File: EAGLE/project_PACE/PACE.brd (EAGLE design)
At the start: 114.5 x 63 mm, 34 parts, among them J3 PTH, U2 MPM3630GQV-P

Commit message: Replace micro usb with usb c
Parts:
- CAM1, CAM2, CAM3, CAM4: value 10118194-0001LF -> USB-C; device USB_Micro_B_v2:AMPHENOL_10118194-0001LF -> USB-C:USB-C
- moved CAM1 77.1 mm to (10.7, 46.0), turned to 270 degrees
- moved CAM2 74.2 mm to (10.7, 32.0), turned to 270 degrees
- moved CAM4 70.9 mm to (77.0, 7.11), turned to 0 degrees
- moved CAM3 70.1 mm to (76.7, 64.8), turned to 180 degrees
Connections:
- net 5VO: now also CAM1.A4, CAM1.A9, CAM2.A4, CAM2.A9, CAM3.A4, CAM3.A9, CAM4.A4, CAM4.A9; no longer CAM1.1, CAM2.1, CAM3.1, CAM4.1
- net GND: now also CAM1.B1, CAM1.B12, CAM2.B1, CAM2.B12, CAM3.B1, CAM3.B12, CAM4.B1, CAM4.B12; no longer CAM1.5, CAM2.5, CAM3.5, CAM4.5
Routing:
- net 5VO: track 234.1 -> 221.7 mm, vias 15 -> 11
- net GND: track 5.51 -> 0.00 mm, vias 17 -> 13

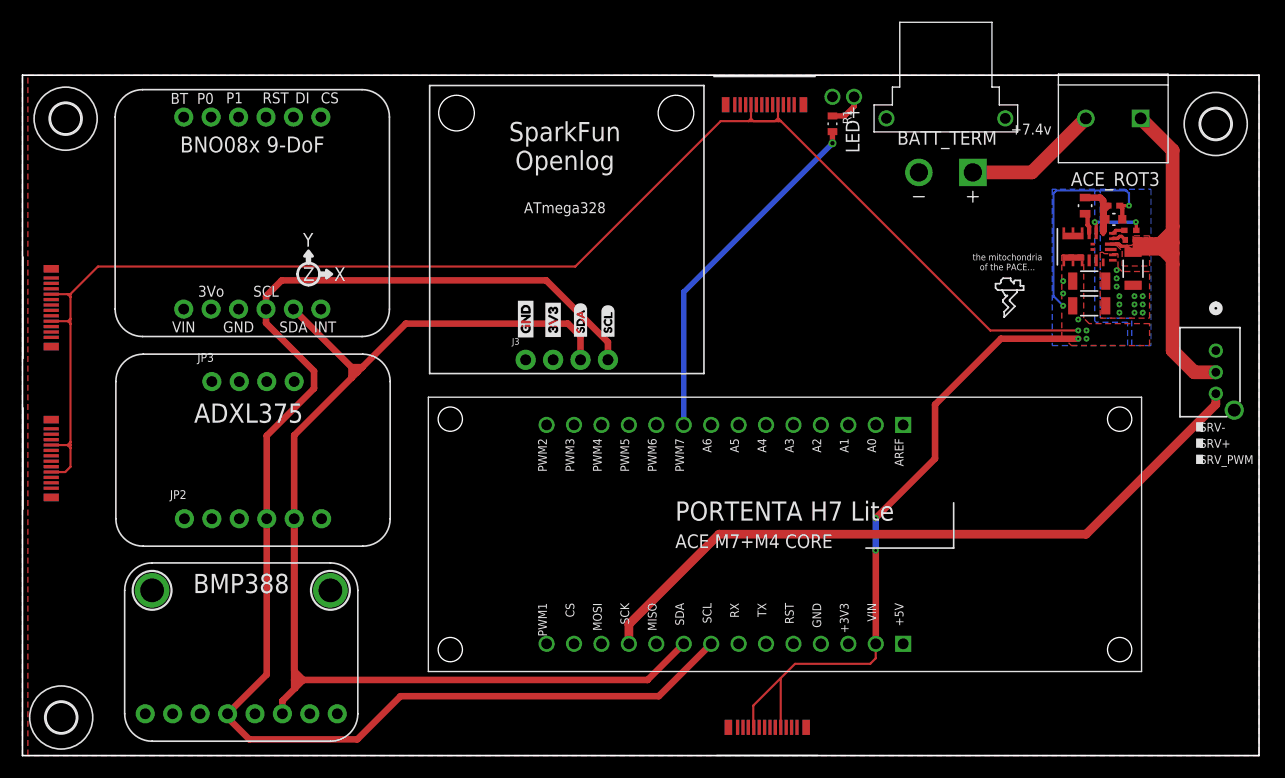
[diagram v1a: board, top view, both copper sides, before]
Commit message: Fix dimensions
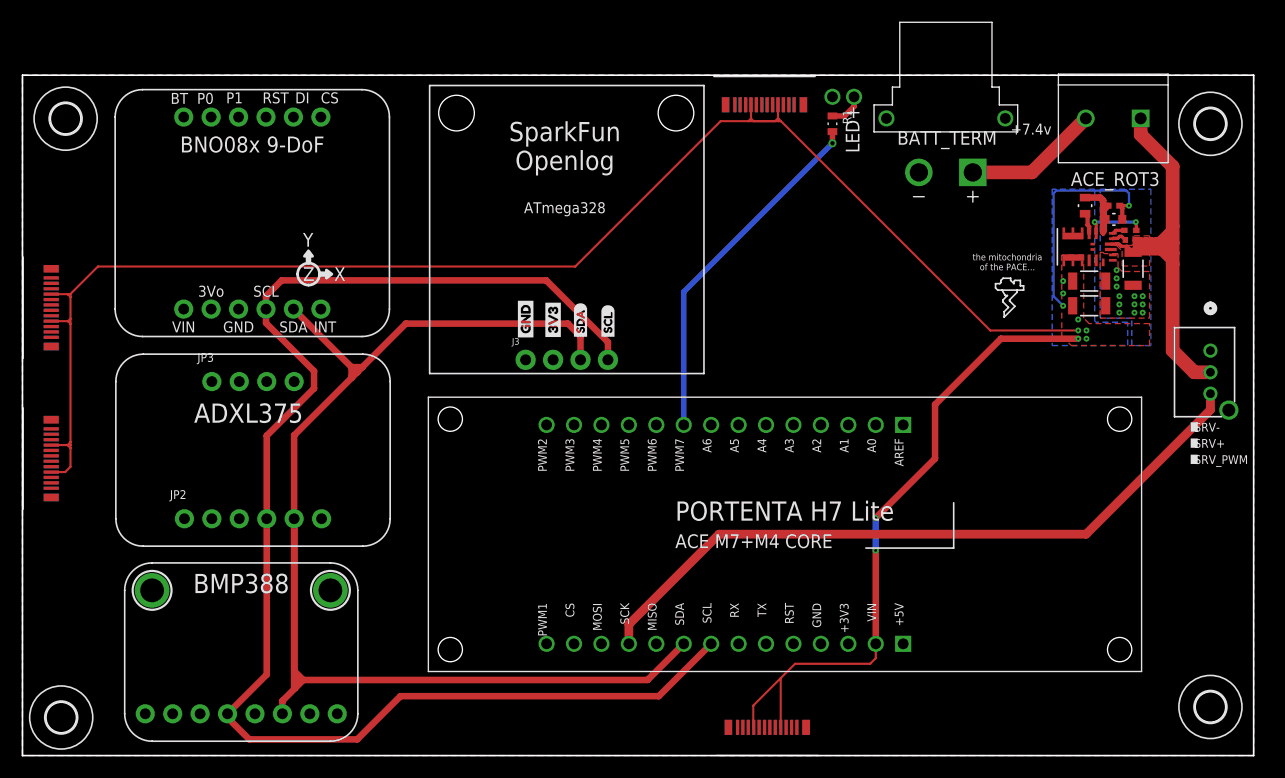
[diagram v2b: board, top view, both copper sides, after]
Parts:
- added U$29: (no value), holes:2,8
- moved SERVOCON 0.50 mm to (118.0, 42.0)
- moved U$14 0.49 mm to (118.0, 63.0)
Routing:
- net 7.4VCC: track 51.7 -> 51.2 mm
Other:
- board size 114.5 x 63 mm -> 114 x 63 mm
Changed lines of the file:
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@@
 <setting verticaltext="up"/>
 </settings>
-<grid distance="10" unitdist="mil" unit="mil" style="lines" multiple="1" display="yes" altdistance="5" altunitdist="mil" altunit="mil"/>
+<grid distance="0.5" unitdist="mm" unit="mm" style="lines" multiple="1" display="yes" altdistance="5" altunitdist="mil" altunit="mil"/>
 <layers>
 <layer number="1" name="Top" color="4" fill="1" visible="yes" active="yes"/>
@@
 <text x="23.885" y="35.321" size="1.778" layer="21">ADXL375</text>
 <dimension x1="22.5" y1="67.5" x2="22.5" y2="4.5" x3="-9" y3="36" textsize="1.778" layer="20"/>
-<wire x1="8" y1="67.5" x2="122.5" y2="67.5" width="0.15" layer="20"/>
-<wire x1="122.5" y1="67.5" x2="122.5" y2="4.5" width="0.15" layer="20"/>
-<wire x1="122.5" y1="4.5" x2="8" y2="4.5" width="0.15" layer="20"/>
+<wire x1="8" y1="67.5" x2="122" y2="67.5" width="0.15" layer="20"/>
+<wire x1="122" y1="67.5" x2="122" y2="4.5" width="0.15" layer="20"/>
+<wire x1="122" y1="4.5" x2="8" y2="4.5" width="0.15" layer="20"/>
 <wire x1="8" y1="4.5" x2="8" y2="67.5" width="0.15" layer="20"/>
 <text x="102.936" y="27.033" size="5.08" layer="22" font="vector" ratio="22" rot="MR45" align="center">P A C E</text>
@@
 ELEMENT</text>
 <text x="99.991" y="7.293" size="1.27" layer="22" font="vector" rot="MR45">v1.0 (now with more ports!)</text>
-<dimension x1="8" y1="67.5" x2="122.5" y2="67.5" x3="65.25" y3="74" textsize="1.778" layer="20"/>
 <text x="99.5" y="62" size="1.016" layer="21" font="vector">+7.4v</text>
-<text x="117" y="31.5" size="0.8128" layer="21" font="vector">SRV_PWM</text>
-<text x="117" y="33" size="0.8128" layer="21" font="vector">SRV+</text>
-<text x="117" y="34.5" size="0.8128" layer="21" font="vector">SRV-</text>
-<text x="116" y="34.5" size="5.08" layer="21" font="vector">.</text>
-<text x="116" y="33" size="5.08" layer="21" font="vector">.</text>
-<text x="116" y="31.5" size="5.08" layer="21" font="vector">.</text>
+<text x="116.5" y="31.5" size="0.8128" layer="21" font="vector">SRV_PWM</text>
+<text x="116.5" y="33" size="0.8128" layer="21" font="vector">SRV+</text>
+<text x="116.5" y="34.5" size="0.8128" layer="21" font="vector">SRV-</text>
+<text x="115.5" y="34.5" size="5.08" layer="21" font="vector">.</text>
+<text x="115.5" y="33" size="5.08" layer="21" font="vector">.</text>
+<text x="115.5" y="31.5" size="5.08" layer="21" font="vector">.</text>
 <text x="85.5" y="60.3" size="1.27" layer="21" font="vector" rot="R90">LED+</text>
 <text x="99.2" y="50.2" size="0.6096" layer="21" font="vector" align="center">the mitochondria
@@
 <wire x1="99.2" y1="47.1" x2="99" y2="47.1" width="0.1524" layer="21"/>
 <wire x1="99" y1="47.1" x2="98.7" y2="47.6" width="0.1524" layer="21"/>
+<dimension x1="8" y1="67.5" x2="122" y2="67.5" x3="65" y3="75.5" textsize="1.778" layer="20"/>
 </plain>
 <attributes>
@@
 <element name="U$10" library="ABX00042" package="MODULE_ABX00042_HEADERS" value="ABX00042_HEADERS_IO" x="78.603" y="24.984" smashed="yes" rot="R270"/>
 <element name="U$13" library="holes" library_urn="urn:adsk.eagle:library:237" package="2,8" package3d_urn="urn:adsk.eagle:package:14271/1" value="" x="11.996" y="63.476" smashed="yes"/>
-<element name="U$14" library="holes" library_urn="urn:adsk.eagle:library:237" package="2,8" package3d_urn="urn:adsk.eagle:package:14271/1" value="" x="118.489" y="62.984" smashed="yes"/>
+<element name="U$14" library="holes" library_urn="urn:adsk.eagle:library:237" package="2,8" package3d_urn="urn:adsk.eagle:package:14271/1" value="" x="118" y="63" smashed="yes"/>
 <element name="U$15" library="holes" library_urn="urn:adsk.eagle:library:237" package="2,8" package3d_urn="urn:adsk.eagle:package:14271/1" value="" x="11.586" y="8.026" smashed="yes"/>
 <element name="U$1" library="microbuilder" package="MOUNTINGHOLE_2.0_PLATED" value="MOUNTINGHOLE2.0" x="20.003" y="19.8" smashed="yes">
@@
 <element name="JP4" library="SparkFun" package="STAND-OFF" value="STAND-OFF" x="48.19" y="63.992" smashed="yes"/>
 <element name="JP5" library="SparkFun" package="STAND-OFF" value="STAND-OFF" x="68.51" y="63.992" smashed="yes"/>
-<element name="SERVOCON" library="3_Pin_JST_XA_Surface_Connector" package="CONN_B03B-PASK-1_(LF)_(SN)_JST" value="B03B-PASK-1_(LF)_(SN)" x="118.5" y="42" smashed="yes" rot="R270">
-<attribute name="COPYRIGHT" value="Copyright (C) 2024 Ultra Librarian. All rights reserved." x="118.5" y="42" size="1.778" layer="27" rot="R270" display="off"/>
-<attribute name="DIGIKEY_PART_NUMBER_1" value="455-1833-ND" x="118.5" y="42" size="1.778" layer="27" rot="R270" display="off"/>
-<attribute name="MANUFACTURER_PART_NUMBER" value="B03B-PASK-1 (LF) (SN)" x="118.5" y="42" size="1.778" layer="27" rot="R270" display="off"/>
-<attribute name="MFR_NAME" value="JST" x="118.5" y="42" size="1.778" layer="27" rot="R270" display="off"/>
-<attribute name="NAME" x="117.865" y="43.27" size="1.27" layer="27" ratio="6" rot="SR270"/>
-<attribute name="VALUE" x="117.865" y="41.7206" size="1.27" layer="27" ratio="6" rot="SR270"/>
+<element name="SERVOCON" library="3_Pin_JST_XA_Surface_Connector" package="CONN_B03B-PASK-1_(LF)_(SN)_JST" value="B03B-PASK-1_(LF)_(SN)" x="118" y="42" smashed="yes" rot="R270">
+<attribute name="COPYRIGHT" value="Copyright (C) 2024 Ultra Librarian. All rights reserved." x="118" y="42" size="1.778" layer="27" rot="R270" display="off"/>
+<attribute name="DIGIKEY_PART_NUMBER_1" value="455-1833-ND" x="118" y="42" size="1.778" layer="27" rot="R270" display="off"/>
+<attribute name="MANUFACTURER_PART_NUMBER" value="B03B-PASK-1 (LF) (SN)" x="118" y="42" size="1.778" layer="27" rot="R270" display="off"/>
+<attribute name="MFR_NAME" value="JST" x="118" y="42" size="1.778" layer="27" rot="R270" display="off"/>
+<attribute name="NAME" x="117.365" y="43.27" size="1.27" layer="27" ratio="6" rot="SR270"/>
+<attribute name="VALUE" x="117.365" y="41.7206" size="1.27" layer="27" ratio="6" rot="SR270"/>
 </element>
 <element name="BATT_TERM" library="XT30PW-F" package="AMASS_XT30PW-F" value="XT30PW-F" x="93.5" y="63.5" smashed="yes">
@@
 <attribute name="SNAPEDA_LINK" value="https://www.snapeda.com/parts/USB-C/Adam+Tech/view-part/?ref=snap" x="76.962" y="7.612" size="1.778" layer="27" display="off"/>
 </element>
+<element name="U$29" library="holes" library_urn="urn:adsk.eagle:library:237" package="2,8" package3d_urn="urn:adsk.eagle:package:14271/1" value="" x="118" y="9" smashed="yes"/>
 </elements>
 <signals>
@@
 <polygon width="0.15" layer="16" rank="3">
 <vertex x="8" y="67.5"/>
-<vertex x="122.5" y="67.5"/>
-<vertex x="122.5" y="4.5"/>
+<vertex x="122" y="67.5"/>
+<vertex x="122" y="4.5"/>
 <vertex x="8" y="4.5"/>
 </polygon>
@@
 <contactref element="JP2" pad="1"/>
 <polygon width="0.15" layer="1" rank="2">
-<vertex x="8.5" y="67.5"/>
-<vertex x="122.5" y="67.5"/>
-<vertex x="122.5" y="4.5"/>
-<vertex x="8.5" y="4.5"/>
+<vertex x="8" y="67.5"/>
+<vertex x="122" y="67.5"/>
+<vertex x="122" y="4.5"/>
+<vertex x="8" y="4.5"/>
 </polygon>
 <contactref element="JP1" pad="1"/>
@@
 <contactref element="ACE_ROT3" pad="1"/>
 <contactref element="SERVOCON" pad="2"/>
-<wire x1="111.54" y1="63.5" x2="114.5" y2="60.54" width="1.27" layer="1"/>
-<wire x1="114.5" y1="60.54" x2="114.5" y2="53.5" width="1.27" layer="1"/>
+<wire x1="114.5" y1="59.04" x2="111.54" y2="62" width="1.27" layer="1"/>
+<wire x1="111.54" y1="63.5" x2="111.54" y2="62" width="1.27" layer="1"/>
+<wire x1="114.5" y1="59.04" x2="114.5" y2="53.5" width="1.27" layer="1"/>
 <wire x1="114.5" y1="53.5" x2="114.5" y2="52" width="1.27" layer="1"/>
 <wire x1="114.5" y1="51" x2="114.5" y2="52" width="1.27" layer="1"/>
@@
 <wire x1="114.5" y1="50" x2="114.5" y2="42" width="1.27" layer="1"/>
 <wire x1="114.5" y1="42" x2="116.5066" y2="39.9934" width="1.27" layer="1"/>
-<wire x1="116.5066" y1="39.9934" x2="118.5" y2="39.9934" width="1.27" layer="1"/>
+<wire x1="116.5066" y1="39.9934" x2="118" y2="39.9934" width="1.27" layer="1"/>
 <wire x1="111.0539" y1="51.3217" x2="110.838" y2="51.1058" width="0.508" layer="1"/>
 <wire x1="111.0539" y1="51.3217" x2="111.0539" y2="52.245" width="0.508" layer="1"/>
@@
 <contactref element="U$10" pad="J25"/>
 <contactref element="SERVOCON" pad="3"/>
-<wire x1="118.5" y1="37.0122" x2="118.5" y2="38.0122" width="0.8128" layer="1"/>
-<wire x1="118.5" y1="37.0122" x2="106.4878" y2="25" width="0.8128" layer="1"/>
+<wire x1="118" y1="36.5122" x2="118" y2="38.0122" width="0.8128" layer="1"/>
+<wire x1="118" y1="36.5122" x2="106.4878" y2="25" width="0.8128" layer="1"/>
 <wire x1="64.1504" y1="16.6504" x2="64.1504" y2="14.8494" width="0.8128" layer="1"/>
 <wire x1="106.4878" y1="25" x2="72.5" y2="25" width="0.8128" layer="1"/>

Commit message: Update USB-C with Molex mfg part
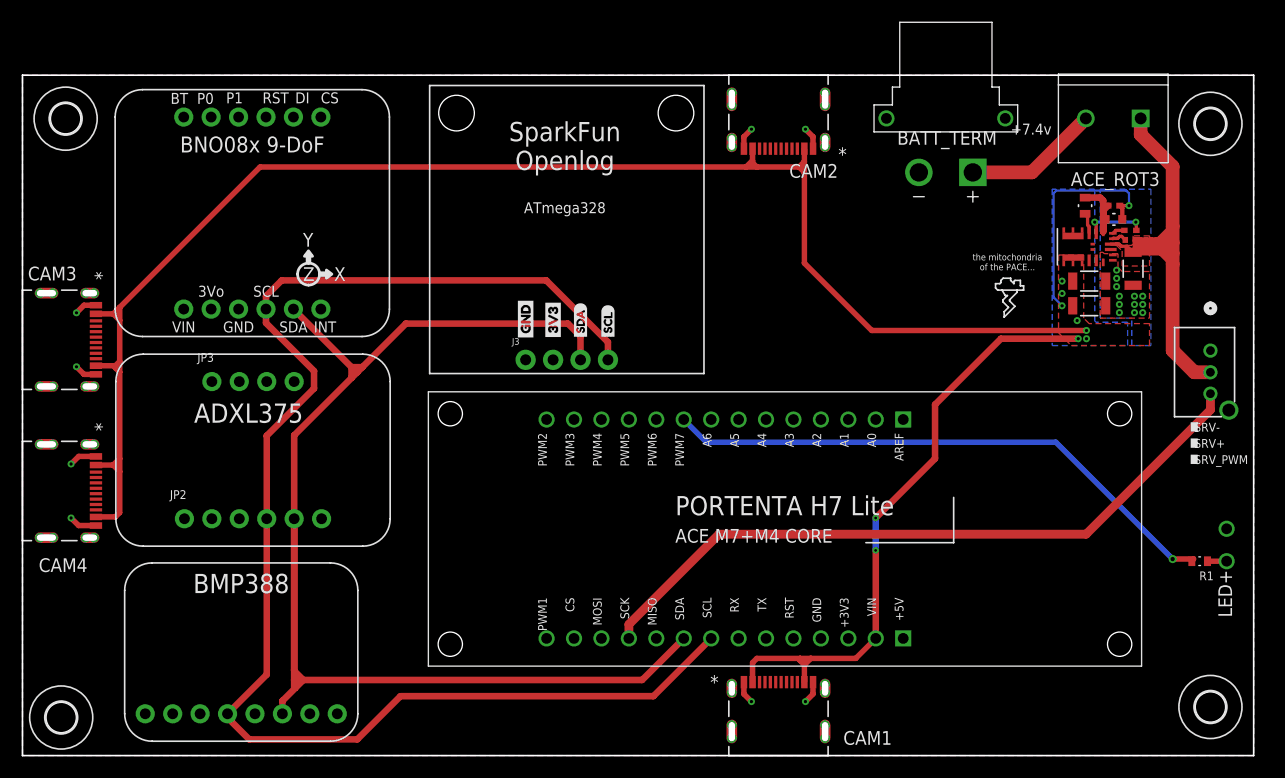
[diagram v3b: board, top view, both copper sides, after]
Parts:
- removed U$1, U$3: MOUNTINGHOLE2.0, microbuilder:MOUNTINGHOLE_2.0_PLATED
- CAM1, CAM2, CAM3, CAM4: value USB-C -> 2171790001; device USB-C:USB-C -> MOLEX-2171790001-USB_C:2171790001_MOL
- moved CAM1 77.3 mm to (78.0, 8.00), turned to 0 degrees
- moved CAM2 74.5 mm to (78.0, 64.0), turned to 180 degrees
- moved CAM4 69.0 mm to (11.5, 29.0), turned to 270 degrees
- moved CAM3 68.7 mm to (11.5, 43.0), turned to 270 degrees
- moved R1 52.9 mm to (117.0, 22.5), turned to 180 degrees
- moved U$10 0.50 mm to (78.6, 25.5)
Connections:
- net 5VO: now also CAM1.A4/B9, CAM1.B4/A9, CAM2.A4/B9, CAM2.B4/A9, CAM3.A4/B9, CAM3.B4/A9, CAM4.A4/B9, CAM4.B4/A9; no longer CAM1.A4, CAM1.A9, CAM2.A4, CAM2.A9, CAM3.A4, CAM3.A9, CAM4.A4, CAM4.A9
- net GND: now also CAM1.A1/B12, CAM1.B1/A12, CAM2.A1/B12, CAM2.B1/A12, CAM3.A1/B12, CAM3.B1/A12, CAM4.A1/B12, CAM4.B1/A12; no longer CAM1.B1, CAM1.B12, CAM2.B1, CAM2.B12, CAM3.B1, CAM3.B12, CAM4.B1, CAM4.B12
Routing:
- net LED: track 32.9 -> 52.8 mm
- net GND: track 0.00 -> 17.7 mm, vias 13 -> 21
- net STAT_LED: track 3.26 -> 1.79 mm
- net 5VO: track 221.7 -> 221.2 mm, vias 11 -> 10
- net SRV_PWM: track 65.4 -> 64.9 mm
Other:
- board text added: "CAM1"
- board text added: "CAM2"
- board text added: "CAM3"
- board text added: "CAM4"
